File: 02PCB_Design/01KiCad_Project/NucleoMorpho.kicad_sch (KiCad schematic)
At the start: 22 parts, among them U11 NUCLEO-G431RB

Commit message: Changed Some Capacitor Sizes, Added Capacitors in Power Gen
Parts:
- renumbered C63 to C69, C64 to C70, C65 to C71, C66 to C72, C67 to C73, C68 to C74, C69 to C75
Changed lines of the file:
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@@
   (symbol (lib_id "Device:C") (at 182.88 81.28 0) (unit 1)
     (in_bom yes) (on_board yes) (dnp no)
-    (property "Reference" "C64" (at 185.42 80.01 0)
+    (property "Reference" "C70" (at 185.42 80.01 0)
       (effects (font (size 1.27 1.27)) (justify left))
     )
@@
       (project "Testplatine"
         (path "/de27a806-41f8-462d-8678-2476d523bbd9/a9fc49c7-f356-4c2b-bdd5-d12f8bcc20f7/ebab6d44-f8ac-40ef-9001-86e6207db3e6"
-          (reference "C64") (unit 1)
+          (reference "C70") (unit 1)
         )
       )
@@
   (symbol (lib_id "Device:C") (at 72.39 101.6 0) (unit 1)
     (in_bom yes) (on_board yes) (dnp no)
-    (property "Reference" "C69" (at 74.93 100.33 0)
+    (property "Reference" "C75" (at 74.93 100.33 0)
       (effects (font (size 1.27 1.27)) (justify left))
     )
@@
       (project "Testplatine"
         (path "/de27a806-41f8-462d-8678-2476d523bbd9/a9fc49c7-f356-4c2b-bdd5-d12f8bcc20f7/ebab6d44-f8ac-40ef-9001-86e6207db3e6"
-          (reference "C69") (unit 1)
+          (reference "C75") (unit 1)
         )
       )
@@
   (symbol (lib_id "Device:C") (at 173.99 85.09 0) (unit 1)
     (in_bom yes) (on_board yes) (dnp no)
-    (property "Reference" "C65" (at 176.53 83.82 0)
+    (property "Reference" "C71" (at 176.53 83.82 0)
       (effects (font (size 1.27 1.27)) (justify left))
     )
@@
       (project "Testplatine"
         (path "/de27a806-41f8-462d-8678-2476d523bbd9/a9fc49c7-f356-4c2b-bdd5-d12f8bcc20f7/ebab6d44-f8ac-40ef-9001-86e6207db3e6"
-          (reference "C65") (unit 1)
+          (reference "C71") (unit 1)
         )
       )
@@
   (symbol (lib_id "Device:C") (at 191.77 77.47 0) (unit 1)
     (in_bom yes) (on_board yes) (dnp no)
-    (property "Reference" "C63" (at 194.31 76.2 0)
+    (property "Reference" "C69" (at 194.31 76.2 0)
       (effects (font (size 1.27 1.27)) (justify left))
     )
@@
       (project "Testplatine"
         (path "/de27a806-41f8-462d-8678-2476d523bbd9/a9fc49c7-f356-4c2b-bdd5-d12f8bcc20f7/ebab6d44-f8ac-40ef-9001-86e6207db3e6"
-          (reference "C63") (unit 1)
+          (reference "C69") (unit 1)
         )
       )
@@
   (symbol (lib_id "Device:C") (at 45.72 90.17 0) (unit 1)
     (in_bom yes) (on_board yes) (dnp no)
-    (property "Reference" "C66" (at 48.26 88.9 0)
+    (property "Reference" "C72" (at 48.26 88.9 0)
       (effects (font (size 1.27 1.27)) (justify left))
     )
@@
       (project "Testplatine"
         (path "/de27a806-41f8-462d-8678-2476d523bbd9/a9fc49c7-f356-4c2b-bdd5-d12f8bcc20f7/ebab6d44-f8ac-40ef-9001-86e6207db3e6"
-          (reference "C66") (unit 1)
+          (reference "C72") (unit 1)
         )
       )
@@
   (symbol (lib_id "Device:C") (at 54.61 93.98 0) (unit 1)
     (in_bom yes) (on_board yes) (dnp no)
-    (property "Reference" "C67" (at 57.15 92.71 0)
+    (property "Reference" "C73" (at 57.15 92.71 0)
       (effects (font (size 1.27 1.27)) (justify left))
     )
@@
       (project "Testplatine"
         (path "/de27a806-41f8-462d-8678-2476d523bbd9/a9fc49c7-f356-4c2b-bdd5-d12f8bcc20f7/ebab6d44-f8ac-40ef-9001-86e6207db3e6"
-          (reference "C67") (unit 1)
+          (reference "C73") (unit 1)
         )
       )
@@
   (symbol (lib_id "Device:C") (at 63.5 97.79 0) (unit 1)
     (in_bom yes) (on_board yes) (dnp no)
-    (property "Reference" "C68" (at 66.04 96.52 0)
+    (property "Reference" "C74" (at 66.04 96.52 0)
       (effects (font (size 1.27 1.27)) (justify left))
     )
@@
       (project "Testplatine"
         (path "/de27a806-41f8-462d-8678-2476d523bbd9/a9fc49c7-f356-4c2b-bdd5-d12f8bcc20f7/ebab6d44-f8ac-40ef-9001-86e6207db3e6"
-          (reference "C68") (unit 1)
-        )
-      )
+          (reference "C74") (unit 1)
+        )
+      )

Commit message: Added Signal Lines
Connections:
- net CURRENT_U: now also R35.1; no longer R32.1
- net CURRENT_V: now also R36.1; no longer R35.1
- net CURRENT_W: now also R34.2; no longer R36.1
- net VOLTAGE_U: now also R32.1; no longer R29.2
- net VOLTAGE_V: now also R29.2; no longer R33.2
- net VOLTAGE_W: now also R33.2; no longer R34.2
- net Current_Comp: now reaches C71.1, R34.1, U11.L_36 (PC1/PB9)
- net Current_Comp: now also U11.L_34 (PB0)
- net at C73.1, R32.2, U11.L_30 (PA1): no longer U11.L_34 (PB0)
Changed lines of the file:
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@@
   (junction (at 63.5 82.55) (diameter 0) (color 0 0 0 0)
   )
-  (junction (at 82.55 69.85) (diameter 0) (color 0 0 0 0)
-  )
   (junction (at 63.5 106.68) (diameter 0) (color 0 0 0 0)
   )
   (junction (at 45.72 67.31) (diameter 0) (color 0 0 0 0)
+  )
+  (junction (at 158.75 72.39) (diameter 0) (color 0 0 0 0)
   )
   (junction (at 191.77 62.23) (diameter 0) (color 0 0 0 0)
@@
     (stroke (width 0) (type default))
   )
-  (wire (pts (xy 82.55 69.85) (xy 105.41 69.85))
+  (wire (pts (xy 54.61 69.85) (xy 105.41 69.85))
     (stroke (width 0) (type default))
   )
@@
     (stroke (width 0) (type default))
   )
+  (wire (pts (xy 172.72 101.6) (xy 158.75 101.6))
+    (stroke (width 0) (type default))
+  )
   (wire (pts (xy 36.83 85.09) (xy 64.77 85.09))
     (stroke (width 0) (type default))
@@
     (stroke (width 0) (type default))
   )
-  (wire (pts (xy 54.61 69.85) (xy 82.55 69.85))
-    (stroke (width 0) (type default))
-  )
   (wire (pts (xy 72.39 97.79) (xy 72.39 85.09))
     (stroke (width 0) (type default))
@@
     (stroke (width 0) (type default))
   )
+  (wire (pts (xy 158.75 72.39) (xy 173.99 72.39))
+    (stroke (width 0) (type default))
+  )
   (wire (pts (xy 149.86 87.63) (xy 146.05 87.63))
     (stroke (width 0) (type default))
   )
-  (wire (pts (xy 82.55 69.85) (xy 82.55 110.49))
-    (stroke (width 0) (type default))
-  )
-  (wire (pts (xy 146.05 72.39) (xy 173.99 72.39))
+  (wire (pts (xy 146.05 72.39) (xy 158.75 72.39))
     (stroke (width 0) (type default))
   )
@@
     (stroke (width 0) (type default))
   )
+  (wire (pts (xy 158.75 101.6) (xy 158.75 72.39))
+    (stroke (width 0) (type default))
+  )
   (wire (pts (xy 104.14 115.57) (xy 105.41 115.57))
     (stroke (width 0) (type default))
@@
     (stroke (width 0) (type default))
   )
-  (wire (pts (xy 146.05 74.93) (xy 157.48 74.93))
+  (wire (pts (xy 146.05 74.93) (xy 161.29 74.93))
     (stroke (width 0) (type default))
   )
@@
     (effects (font (size 1.1 1.1)) (justify left bottom))
   )
-  (hierarchical_label "CURRENT_W" (shape input) (at 36.83 85.09 180) (fields_autoplaced)
-    (effects (font (size 1.27 1.27)) (justify right))
+  (label "Current_Comp" (at 172.72 101.6 0) (fields_autoplaced)
+    (effects (font (size 1.27 1.27)) (justify left bottom))
+  )
+  (label "Current_Comp" (at 82.55 110.49 180) (fields_autoplaced)
+    (effects (font (size 1.27 1.27)) (justify right bottom))
+  )
+  (hierarchical_label "CURRENT_W" (shape input) (at 200.66 72.39 0) (fields_autoplaced)
+    (effects (font (size 1.27 1.27)) (justify left))
   )
   (hierarchical_label "FDCAN_TX" (shape input) (at 35.56 133.35 180) (fields_autoplaced)
@@
     (effects (font (size 1.27 1.27)) (justify right))
   )
-  (hierarchical_label "CURRENT_U" (shape input) (at 36.83 69.85 180) (fields_autoplaced)
+  (hierarchical_label "CURRENT_U" (shape input) (at 36.83 82.55 180) (fields_autoplaced)
     (effects (font (size 1.27 1.27)) (justify right))
   )
@@
     (effects (font (size 1.27 1.27)) (justify left))
   )
-  (hierarchical_label "VOLTAGE_V" (shape input) (at 200.66 69.85 0) (fields_autoplaced)
+  (hierarchical_label "VOLTAGE_V" (shape input) (at 200.66 62.23 0) (fields_autoplaced)
     (effects (font (size 1.27 1.27)) (justify left))
   )
@@
     (effects (font (size 1.27 1.27)) (justify left))
   )
-  (hierarchical_label "VOLTAGE_W" (shape input) (at 200.66 72.39 0) (fields_autoplaced)
-    (effects (font (size 1.27 1.27)) (justify left))
-  )
-  (hierarchical_label "PWM_HI_W" (shape input) (at 157.48 74.93 0) (fields_autoplaced)
+  (hierarchical_label "VOLTAGE_W" (shape input) (at 200.66 69.85 0) (fields_autoplaced)
+    (effects (font (size 1.27 1.27)) (justify left))
+  )
+  (hierarchical_label "PWM_HI_W" (shape input) (at 161.29 74.93 0) (fields_autoplaced)
     (effects (font (size 1.27 1.27)) (justify left))
   )
@@
     (effects (font (size 1.27 1.27)) (justify right))
   )
-  (hierarchical_label "VOLTAGE_U" (shape input) (at 200.66 62.23 0) (fields_autoplaced)
-    (effects (font (size 1.27 1.27)) (justify left))
-  )
-  (hierarchical_label "CURRENT_V" (shape input) (at 36.83 82.55 180) (fields_autoplaced)
-    (effects (font (size 1.27 1.27)) (justify right))
-  )
+  (hierarchical_label "VOLTAGE_U" (shape input) (at 36.83 69.85 180) (fields_autoplaced)
+    (effects (font (size 1.27 1.27)) (justify right))
+  )
+  (hierarchical_label "CURRENT_V" (shape input) (at 36.83 85.09 180) (fields_autoplaced)
+    (effects (font (size 1.27 1.27)) (justify right))
+  )

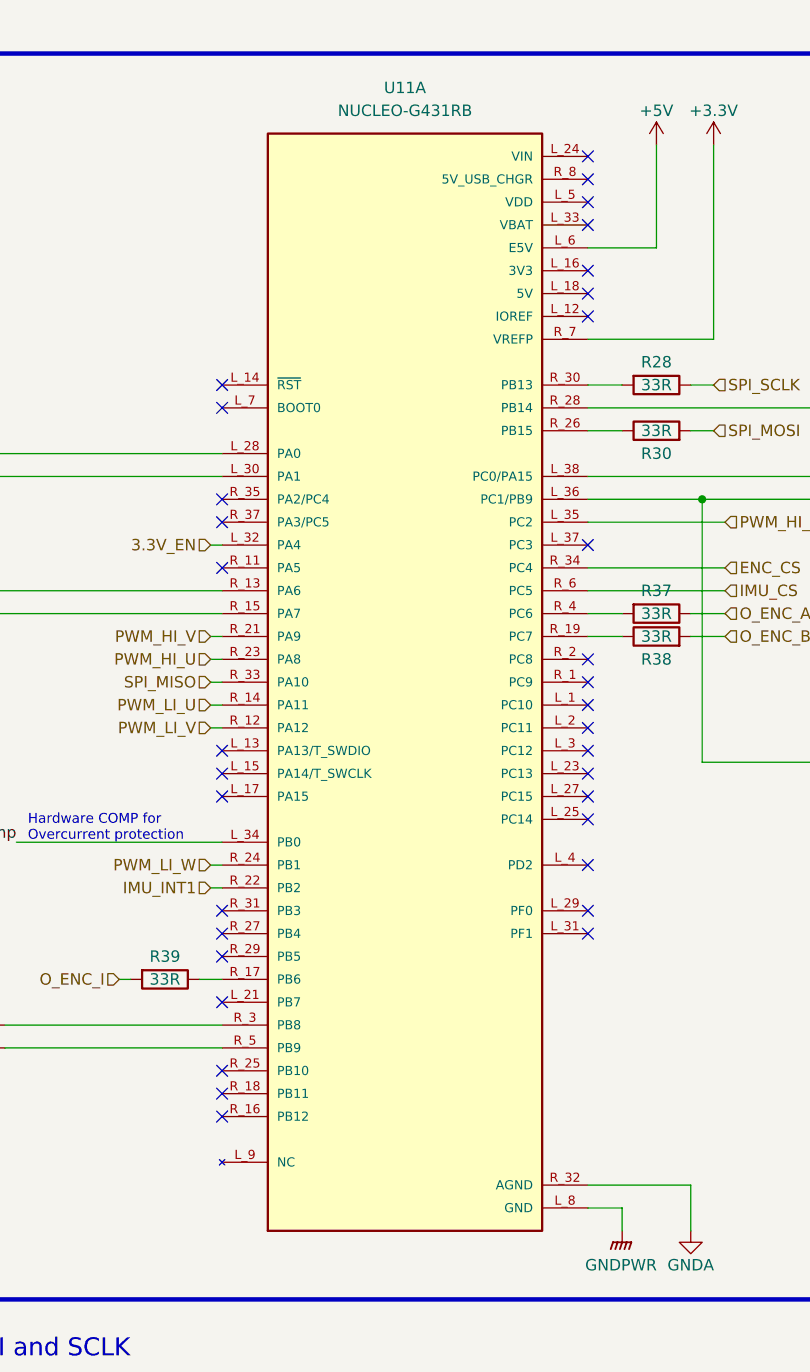
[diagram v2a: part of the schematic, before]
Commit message: edited footprints
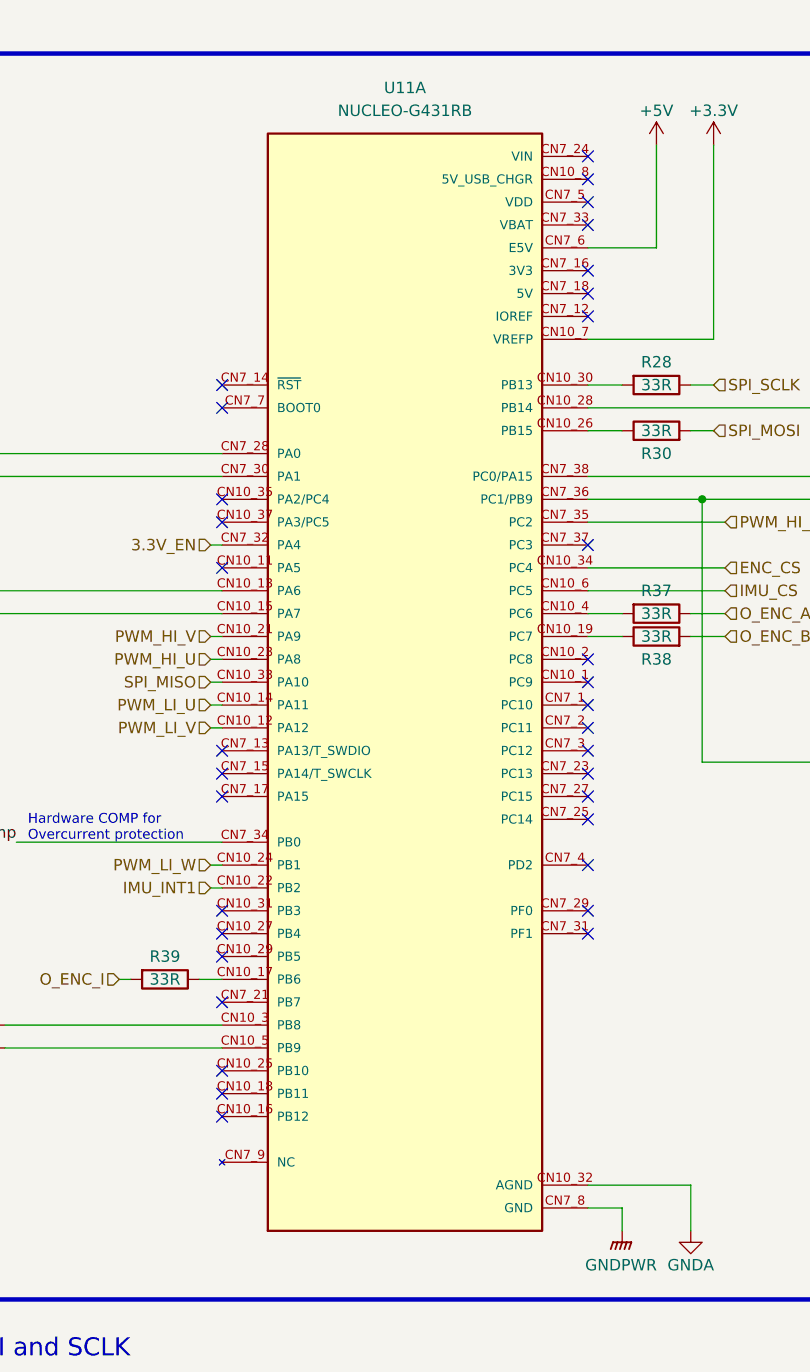
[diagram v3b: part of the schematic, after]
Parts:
- U11: footprint footprints:NucleoMorphoG431RB -> MyFootprintLib:NucleoCN7CN10
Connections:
- net +3.3V: now also U11.CN10_7 (VREFP); no longer U11.R_7 (VREFP)
- net +5V: now also U11.CN7_6 (E5V); no longer U11.L_6 (E5V)
- net 3.3V_EN: now also U11.CN7_32 (PA4); no longer U11.L_32 (PA4)
- net Current_Comp: now also U11.CN7_34 (PB0), U11.CN7_36 (PC1/PB9); no longer U11.L_34 (PB0), U11.L_36 (PC1/PB9)
- net ENC_CS: now also U11.CN10_34 (PC4); no longer U11.R_34 (PC4)
- net GND: now also U11.CN10_20 (GND), U11.CN10_9 (GND), U11.CN7_19 (GND), U11.CN7_20 (GND), U11.CN7_22 (GND), U11.CN7_8 (GND); no longer U11.L_19 (GND), U11.L_20 (GND), U11.L_22 (GND), U11.L_8 (GND), U11.R_20 (GND), U11.R_9 (GND)
- net GNDA: now also U11.CN10_32 (AGND); no longer U11.R_32 (AGND)
- net IMU_CS: now also U11.CN10_6 (PC5); no longer U11.R_6 (PC5)
- net IMU_INT1: now also U11.CN10_22 (PB2); no longer U11.R_22 (PB2)
- net PWM_HI_U: now also U11.CN10_23 (PA8); no longer U11.R_23 (PA8)
- net PWM_HI_V: now also U11.CN10_21 (PA9); no longer U11.R_21 (PA9)
- net PWM_HI_W: now also U11.CN7_35 (PC2); no longer U11.L_35 (PC2)
- net PWM_LI_U: now also U11.CN10_14 (PA11); no longer U11.R_14 (PA11)
- net PWM_LI_V: now also U11.CN10_12 (PA12); no longer U11.R_12 (PA12)
- net PWM_LI_W: now also U11.CN10_24 (PB1); no longer U11.R_24 (PB1)
- net SPI_MISO: now also U11.CN10_33 (PA10); no longer U11.R_33 (PA10)
- net at R38.1: now also U11.CN10_19 (PC7); no longer U11.R_19 (PC7)
- net at C73.1, R32.2: now also U11.CN7_30 (PA1); no longer U11.L_30 (PA1)
- net at R41.2: now also U11.CN10_5 (PB9); no longer U11.R_5 (PB9)
- net at C70.1, R33.1: now also U11.CN7_38 (PC0/PA15); no longer U11.L_38 (PC0/PA15)
- net at R28.2: now also U11.CN10_30 (PB13); no longer U11.R_30 (PB13)
- net at R39.1: now also U11.CN10_17 (PB6); no longer U11.R_17 (PB6)
- net at R40.2: now also U11.CN10_3 (PB8); no longer U11.R_3 (PB8)
- net at R37.2: now also U11.CN10_4 (PC6); no longer U11.R_4 (PC6)
- net at R30.1: now also U11.CN10_26 (PB15); no longer U11.R_26 (PB15)
- net at C75.1, R36.2: now also U11.CN10_15 (PA7); no longer U11.R_15 (PA7)
- net at C72.1, R31.2: now also U11.CN7_28 (PA0); no longer U11.L_28 (PA0)
- net at C74.1, R35.2: now also U11.CN10_13 (PA6); no longer U11.R_13 (PA6)
- net at C69.1, R29.1: now also U11.CN10_28 (PB14); no longer U11.R_28 (PB14)
- new net: U11.CN10_10 (NC), U11.CN10_36 (NC), U11.CN10_38 (NC), U11.CN7_10 (NC), U11.CN7_11 (NC), U11.CN7_26 (NC), U11.CN7_9 (NC)
